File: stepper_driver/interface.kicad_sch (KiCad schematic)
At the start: 16 parts, among them J1 Conn_FFC_20_Pin_1mm_bottom-ZF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, J2 Conn_TERM_HDR_01x08_Pin_3.5MM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, U1 LVDS_4-4_HALF_DS91M040TSQE, U2 LVDS_4-4_HALF_DS91M040TSQE, U2 MAX6817

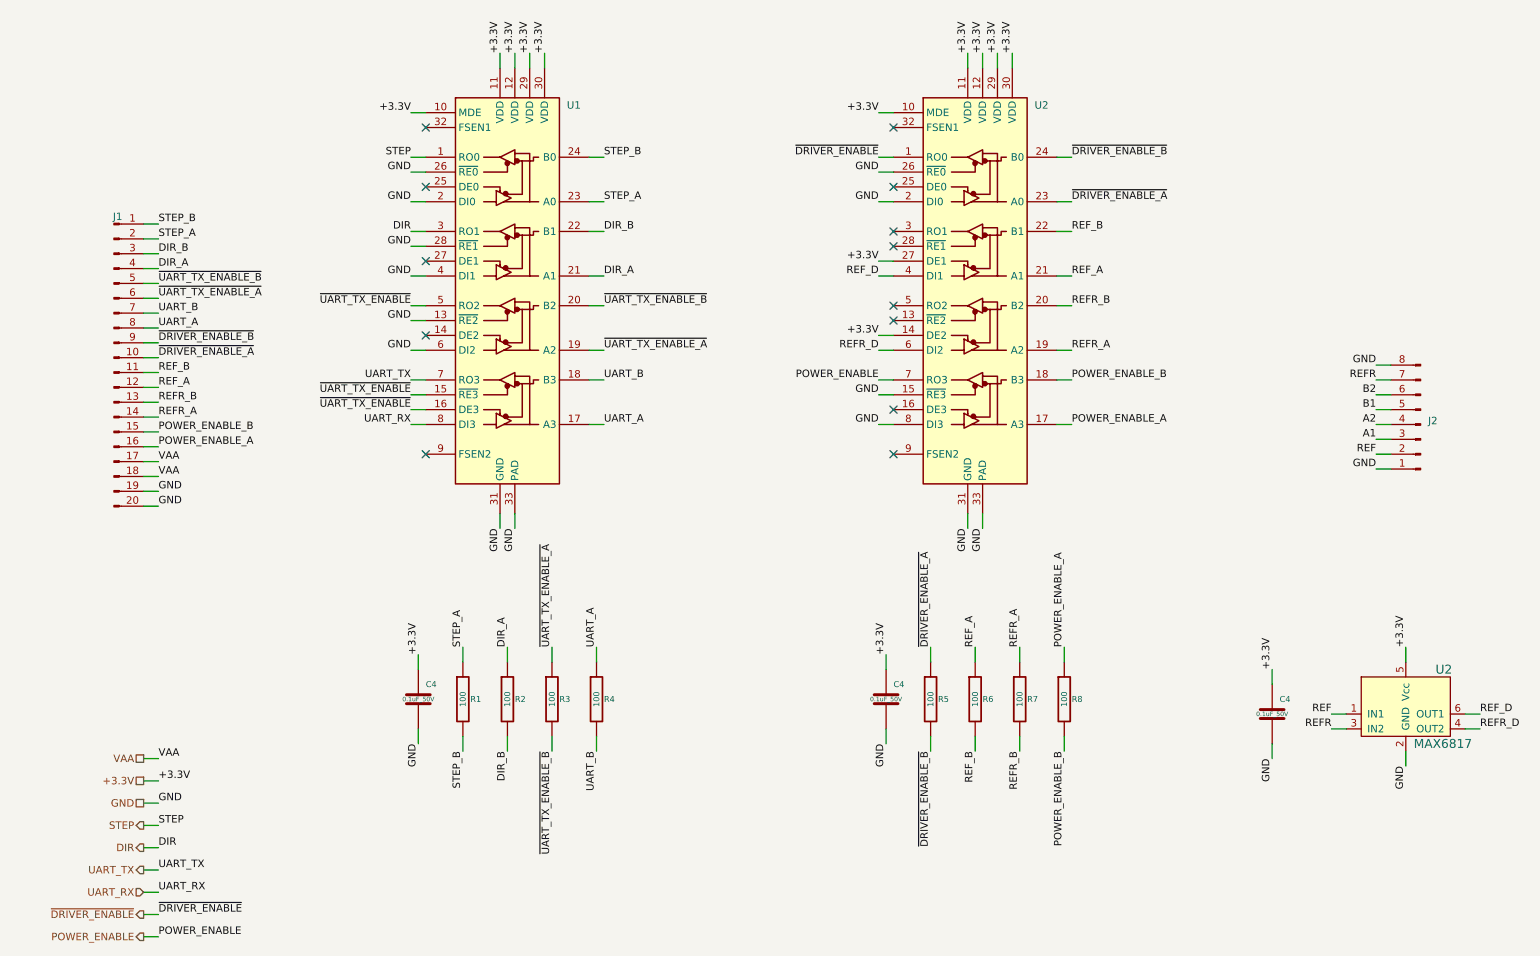
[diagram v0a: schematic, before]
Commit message: power_enable -> standby
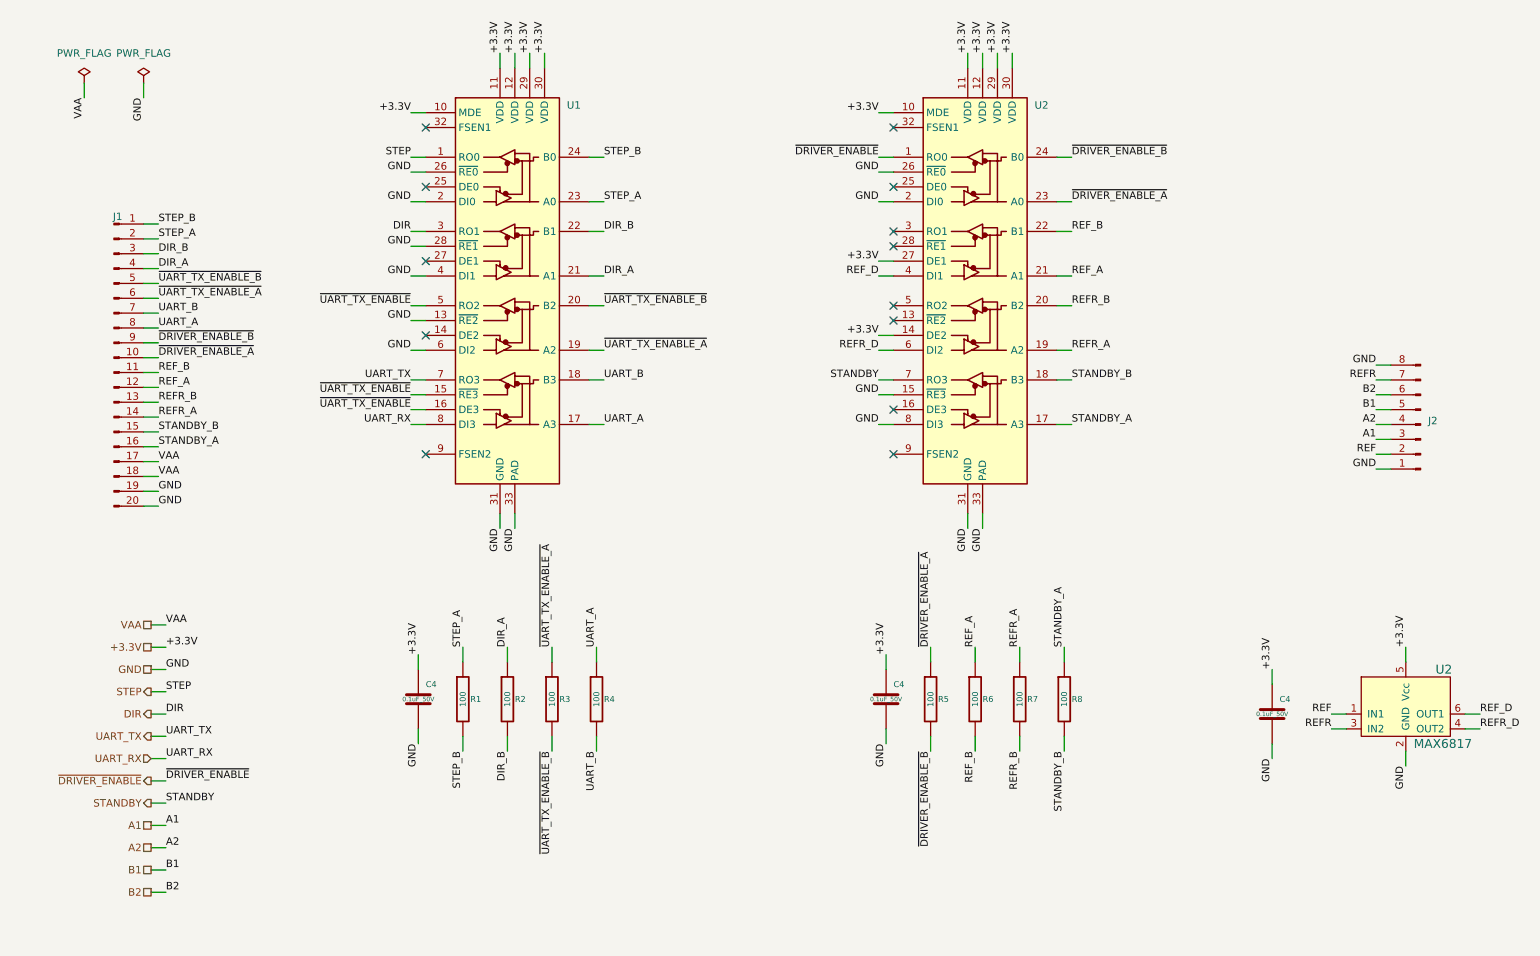
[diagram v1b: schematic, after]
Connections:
- net POWER_ENABLE renamed STANDBY
- net POWER_ENABLE_A renamed STANDBY_A
- net POWER_ENABLE_B renamed STANDBY_B

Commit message: Move pins
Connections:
- net +3.3V: now also U2.16 (DE3); no longer U2.27 (DE1)
- net GND: now also U2.28 (~{RE1}), U2.4 (DI1); no longer U2.15 (~{RE3}), U2.8 (DI3)
- net REFR_A: now also J1.16 (Pin_16), R8.1, U2.17 (A3); no longer J1.14 (Pin_14), R7.1, U2.19 (A2)
- net REFR_B: now also J1.15 (Pin_15), R8.2, U2.18 (B3); no longer J1.13 (Pin_13), R7.2, U2.20 (B2)
- net REFR_D: now also U2.8 (DI3); no longer U2.6 (DI2)
- net REF_A: now also J1.14 (Pin_14), R7.1, U2.19 (A2); no longer J1.12 (Pin_12), R6.1, U2.21 (A1)
- net REF_B: now also J1.13 (Pin_13), R7.2, U2.20 (B2); no longer J1.11 (Pin_11), R6.2, U2.22 (B1)
- net REF_D: now also U2.6 (DI2); no longer U2.4 (DI1)
- net STANDBY: now also U2.3 (RO1); no longer U2.7 (RO3)
- net STANDBY_A: now also J1.12 (Pin_12), R6.1, U2.21 (A1); no longer J1.16 (Pin_16), R8.1, U2.17 (A3)
- net STANDBY_B: now also J1.11 (Pin_11), R6.2, U2.22 (B1); no longer J1.15 (Pin_15), R8.2, U2.18 (B3)

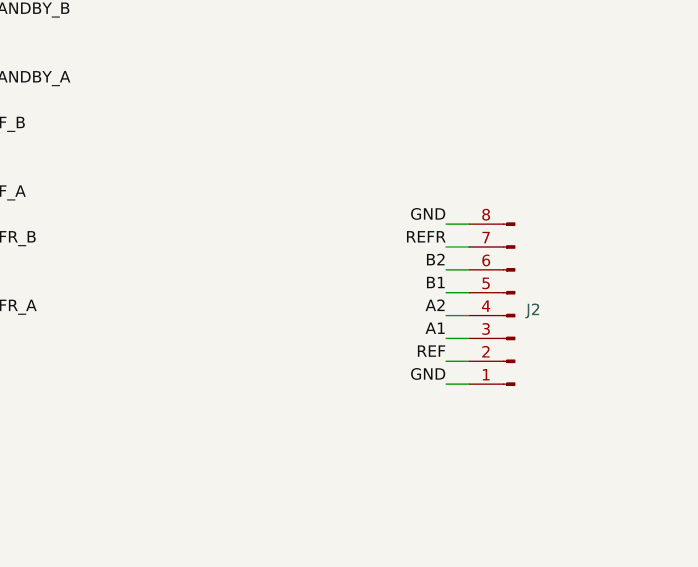
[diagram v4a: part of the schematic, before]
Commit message: Change 8 pin connector
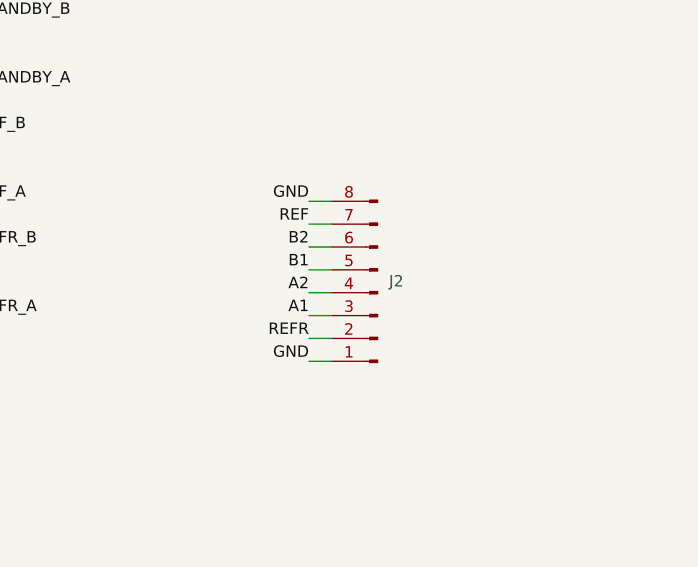
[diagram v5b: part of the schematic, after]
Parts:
- removed J2: Conn_TERM_HDR_01x08_Pin_3.5MM_Horizontal, Janelia:TERM_HDR_01x08_Pin_Horizontal_3.5MM_1844278, symbol Janelia:Conn_TERM_HDR_01x08_Pin_3.5MM_Horizontal
- added J2: Conn_TERM_HDR_01x08_Pin_2.5MM_Horizontal_SMD, Janelia:TERM_HDR_01x08_Pin_Horizontal_2.5MM_1778829, symbol Janelia:Conn_TERM_HDR_01x08_Pin_2.5MM_Horizontal_SMD
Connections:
- net A1: now also J2.3 (Pin_3)
- net A2: now also J2.4 (Pin_4)
- net B1: now also J2.5 (Pin_5)
- net B2: now also J2.6 (Pin_6)
- net GND: now also J2.1 (Pin_1), J2.8 (Pin_8)
- net REF: now also J2.7 (Pin_7)
- net REFR: now also J2.2 (Pin_2)
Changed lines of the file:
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@@
-    (stroke (width 0) (type default))
-  )
-  (wire (pts (xy 252.73 78.74) (xy 250.19 78.74))
     (stroke (width 0) (type default))
   )
@@
     (stroke (width 0) (type default))
   )
-  (wire (pts (xy 252.73 96.52) (xy 250.19 96.52))
+  (wire (pts (xy 237.49 76.2) (xy 234.95 76.2))
     (stroke (width 0) (type default))
   )
@@
     (stroke (width 0) (type default))
   )
-  (wire (pts (xy 252.73 83.82) (xy 250.19 83.82))
+  (wire (pts (xy 237.49 81.28) (xy 234.95 81.28))
     (stroke (width 0) (type default))
   )
@@
     (stroke (width 0) (type default))
   )
-  (wire (pts (xy 252.73 91.44) (xy 250.19 91.44))
+  (wire (pts (xy 237.49 88.9) (xy 234.95 88.9))
     (stroke (width 0) (type default))
   )
@@
     (stroke (width 0) (type default))
   )
-  (wire (pts (xy 252.73 88.9) (xy 250.19 88.9))
+  (wire (pts (xy 237.49 86.36) (xy 234.95 86.36))
     (stroke (width 0) (type default))
   )
@@
     (stroke (width 0) (type default))
   )
+  (wire (pts (xy 237.49 93.98) (xy 234.95 93.98))
+    (stroke (width 0) (type default))
+  )
   (wire (pts (xy 166.37 140.97) (xy 166.37 143.51))
     (stroke (width 0) (type default))
@@
     (stroke (width 0) (type default))
   )
-  (wire (pts (xy 252.73 93.98) (xy 250.19 93.98))
+  (wire (pts (xy 237.49 78.74) (xy 234.95 78.74))
     (stroke (width 0) (type default))
   )
@@
     (stroke (width 0) (type default))
   )
-  (wire (pts (xy 252.73 81.28) (xy 250.19 81.28))
+  (wire (pts (xy 237.49 91.44) (xy 234.95 91.44))
     (stroke (width 0) (type default))
   )
@@
     (stroke (width 0) (type default))
   )
-  (wire (pts (xy 252.73 86.36) (xy 250.19 86.36))
+  (wire (pts (xy 237.49 83.82) (xy 234.95 83.82))
     (stroke (width 0) (type default))
   )
@@
     (effects (font (size 1.27 1.27)) (justify right bottom))
   )
-  (label "A2" (at 250.19 88.9 180) (fields_autoplaced)
+  (label "A2" (at 234.95 86.36 180) (fields_autoplaced)
     (effects (font (size 1.27 1.27)) (justify right bottom))
   )
@@
     (effects (font (size 1.27 1.27)) (justify left bottom))
   )
-  (label "REFR" (at 250.19 81.28 180) (fields_autoplaced)
+  (label "REFR" (at 234.95 91.44 180) (fields_autoplaced)
     (effects (font (size 1.27 1.27)) (justify right bottom))
   )
@@
     (effects (font (size 1.27 1.27)) (justify right bottom))
   )
-  (label "GND" (at 250.19 96.52 180) (fields_autoplaced)
+  (label "GND" (at 234.95 76.2 180) (fields_autoplaced)
     (effects (font (size 1.27 1.27)) (justify right bottom))
   )
@@
     (effects (font (size 1.27 1.27)) (justify left bottom))
   )
-  (label "B1" (at 250.19 86.36 180) (fields_autoplaced)
+  (label "B1" (at 234.95 83.82 180) (fields_autoplaced)
     (effects (font (size 1.27 1.27)) (justify right bottom))
   )
@@
     (effects (font (size 1.27 1.27)) (justify right bottom))
   )
-  (label "REF" (at 250.19 93.98 180) (fields_autoplaced)
+  (label "REF" (at 234.95 78.74 180) (fields_autoplaced)
     (effects (font (size 1.27 1.27)) (justify right bottom))
   )
@@
     (effects (font (size 1.27 1.27)) (justify left bottom))
   )
-  (label "A1" (at 250.19 91.44 180) (fields_autoplaced)
+  (label "A1" (at 234.95 88.9 180) (fields_autoplaced)
     (effects (font (size 1.27 1.27)) (justify right bottom))
   )
@@
     (effects (font (size 1.27 1.27)) (justify left bottom))
   )
+  (label "GND" (at 234.95 93.98 180) (fields_autoplaced)
+    (effects (font (size 1.27 1.27)) (justify right bottom))
+  )
   (label "+3.3V" (at 85.09 35.56 180) (fields_autoplaced)
     (effects (font (size 1.27 1.27)) (justify right bottom))
@@
     (effects (font (size 1.27 1.27)) (justify left bottom))
   )
-  (label "GND" (at 250.19 78.74 180) (fields_autoplaced)
-    (effects (font (size 1.27 1.27)) (justify right bottom))
-  )
-  (label "B2" (at 250.19 83.82 180) (fields_autoplaced)
+  (label "B2" (at 234.95 81.28 180) (fields_autoplaced)
     (effects (font (size 1.27 1.27)) (justify right bottom))
   )
@@
     )
   )
-  (symbol (lib_id "Janelia:Conn_TERM_HDR_01x08_Pin_3.5MM_Horizontal") (at 257.81 88.9 180) (unit 1)
+  (symbol (lib_id "Janelia:R_100_0402") (at 93.98 135.89 0) (unit 1)
+    (in_bom yes) (on_board yes) (dnp no)
+    (property "Reference" "R1" (at 95.25 135.89 0)
+      (effects (font (size 1.016 1.016)) (justify left))
+    )
+    (property "Value" "100" (at 93.98 135.89 90)
+      (effects (font (size 1.016 1.016)))
+    )
+    (property "Footprint" "Janelia:R_0402_1005Metric" (at 92.202 135.89 90)
+      (effects (font (size 0.762 0.762)) hide)
+    )
+    (property "Datasheet" "" (at 93.98 135.89 0)
+      (effects (font (size 0.762 0.762)))
+    )
+    (property "Vendor" "Digi-Key" (at 98.552 133.35 90)
+      (effects (font (size 1.524 1.524)) hide)
+    )
+    (property "Vendor Part Number" "RMCF0402FT100RCT-ND" (at 101.092 130.81 90)
+      (effects (font (size 1.524 1.524)) hide)
+    )
+    (property "Description" "RES 100 OHM 1% 1/16W" (at 103.632 128.27 90)
+      (effects (font (size 1.524 1.524)) hide)
+    )
+    (property "Package" "0402" (at 93.98 135.89 0)
+      (effects (font (size 1.27 1.27)) hide)
+    )
+    (property "Manufacturer" "Stackpole Electronics Inc" (at 93.98 135.89 0)
+      (effects (font (size 1.27 1.27)) hide)
+    )
+    (property "Manufacturer Part Number" "RMCF0402FT100R" (at 93.98 135.89 0)
+      (effects (font (size 1.27 1.27)) hide)
+    )
+    (pin "1")
+    (pin "2")
+    (instances
+      (project "stepper_driver"
+        (path "/cc457ebc-4af6-4663-b19f-8cb38f061cb4/25e66ddf-c258-4744-8ed9-64f4b44995b0"
+          (reference "R1") (unit 1)
+        )
+      )
+    )
+  )
+  (symbol (lib_id "Janelia:Conn_TERM_HDR_01x08_Pin_2.5MM_Horizontal_SMD") (at 242.57 86.36 180) (unit 1)
     (in_bom yes) (on_board yes) (dnp no) (fields_autoplaced)
-    (property "Reference" "J2" (at 259.08 88.265 0)
+    (property "Reference" "J2" (at 243.84 85.09 0)
       (effects (font (size 1.27 1.27)) (justify right))
     )
-    (property "Value" "Conn_TERM_HDR_01x08_Pin_3.5MM_Horizontal" (at 257.81 76.2 0)
-      (effects (font (size 1.27 1.27)) hide)
-    )
-    (property "Footprint" "Janelia:TERM_HDR_01x08_Pin_Horizontal_3.5MM_1844278" (at 257.81 124.46 0)
-      (effects (font (size 1.27 1.27)) hide)
-    )
-    (property "Datasheet" "~" (at 257.81 88.9 0)
-      (effects (font (size 1.27 1.27)) hide)
-    )
-    (property "Manufacturer" "Phoenix Contact" (at 257.81 121.92 0)
-      (effects (font (size 1.27 1.27)) hide)
-    )
-    (property "Manufacturer Part Number" "1844278" (at 257.81 116.84 0)
-      (effects (font (size 1.27 1.27)) hide)
-    )
-    (property "Description" "TERM BLOCK HDR 8POS 90DEG 3.5MM" (at 257.81 114.3 0)
-      (effects (font (size 1.27 1.27)) hide)
-    )
-    (property "Vendor" "Digi-Key" (at 257.81 119.38 0)
-      (effects (font (size 1.27 1.27)) hide)
-    )
-    (property "Vendor Part Number" "277-5763-ND" (at 257.81 111.76 0)
-      (effects (font (size 1.27 1.27)) hide)
-    )
-    (property "Sim.Enable" "0" (at 257.81 88.9 0)
+    (property "Value" "Conn_TERM_HDR_01x08_Pin_2.5MM_Horizontal_SMD" (at 242.57 73.66 0)
+      (effects (font (size 1.27 1.27)) hide)
+    )
+    (property "Footprint" "Janelia:TERM_HDR_01x08_Pin_Horizontal_2.5MM_1778829" (at 242.57 121.92 0)
+      (effects (font (size 1.27 1.27)) hide)
+    )
+    (property "Datasheet" "" (at 242.57 106.68 0)
+      (effects (font (size 1.27 1.27)) hide)
+    )
+    (property "Manufacturer" "Phoenix Contact" (at 242.57 119.38 0)
+      (effects (font (size 1.27 1.27)) hide)
+    )
+    (property "Manufacturer Part Number" "1778829" (at 242.57 114.3 0)
+      (effects (font (size 1.27 1.27)) hide)
+    )
+    (property "Description" "TERM BLOCK HDR 8POS 90DEG 2.5MM" (at 242.57 111.76 0)
+      (effects (font (size 1.27 1.27)) hide)
+    )
+    (property "Vendor" "Digi-Key" (at 242.57 116.84 0)
+      (effects (font (size 1.27 1.27)) hide)
+    )
+    (property "Vendor Part Number" "277-2321-1-ND" (at 242.57 109.22 0)
+      (effects (font (size 1.27 1.27)) hide)
+    )
+    (property "Sim.Enable" "0" (at 242.57 86.36 0)
       (effects (font (size 1.27 1.27)) hide)
     )
@@
     (instances
       (project "stepper_driver"
-        (path "/cc457ebc-4af6-4663-b19f-8cb38f061cb4"
-          (reference "J2") (unit 1)
-        )
         (path "/cc457ebc-4af6-4663-b19f-8cb38f061cb4/25e66ddf-c258-4744-8ed9-64f4b44995b0"
           (reference "J2") (unit 1)
         )
       )
-    )
-  )
-  (symbol (lib_id "Janelia:R_100_0402") (at 93.98 135.89 0) (unit 1)
-    (in_bom yes) (on_board yes) (dnp no)
-    (property "Reference" "R1" (at 95.25 135.89 0)
-      (effects (font (size 1.016 1.016)) (justify left))
-    )
-    (property "Value" "100" (at 93.98 135.89 90)
-      (effects (font (size 1.016 1.016)))
-    )
-    (property "Footprint" "Janelia:R_0402_1005Metric" (at 92.202 135.89 90)
-      (effects (font (size 0.762 0.762)) hide)
-    )
-    (property "Datasheet" "" (at 93.98 135.89 0)
-      (effects (font (size 0.762 0.762)))
-    )
-    (property "Vendor" "Digi-Key" (at 98.552 133.35 90)
-      (effects (font (size 1.524 1.524)) hide)
-    )
-    (property "Vendor Part Number" "RMCF0402FT100RCT-ND" (at 101.092 130.81 90)
-      (effects (font (size 1.524 1.524)) hide)
-    )
-    (property "Description" "RES 100 OHM 1% 1/16W" (at 103.632 128.27 90)
-      (effects (font (size 1.524 1.524)) hide)
-    )
-    (property "Package" "0402" (at 93.98 135.89 0)
-      (effects (font (size 1.27 1.27)) hide)
-    )
-    (property "Manufacturer" "Stackpole Electronics Inc" (at 93.98 135.89 0)
-      (effects (font (size 1.27 1.27)) hide)
-    )
-    (property "Manufacturer Part Number" "RMCF0402FT100R" (at 93.98 135.89 0)
-      (effects (font (size 1.27 1.27)) hide)
-    )
-    (pin "1")
-    (pin "2")
-    (instances
-      (project "stepper_driver"
-        (path "/cc457ebc-4af6-4663-b19f-8cb38f061cb4/25e66ddf-c258-4744-8ed9-64f4b44995b0"
-          (reference "R1") (unit 1)
-        )
-      )
